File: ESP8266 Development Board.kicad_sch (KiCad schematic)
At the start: 21 parts, among them J1 Barrel_Jack, J2 Conn_01x01_Female, J3 Conn_01x01_Female, SW1 SW_SPST, SW2 SW_Push, U1 ESP8266-12E_Dev_Board

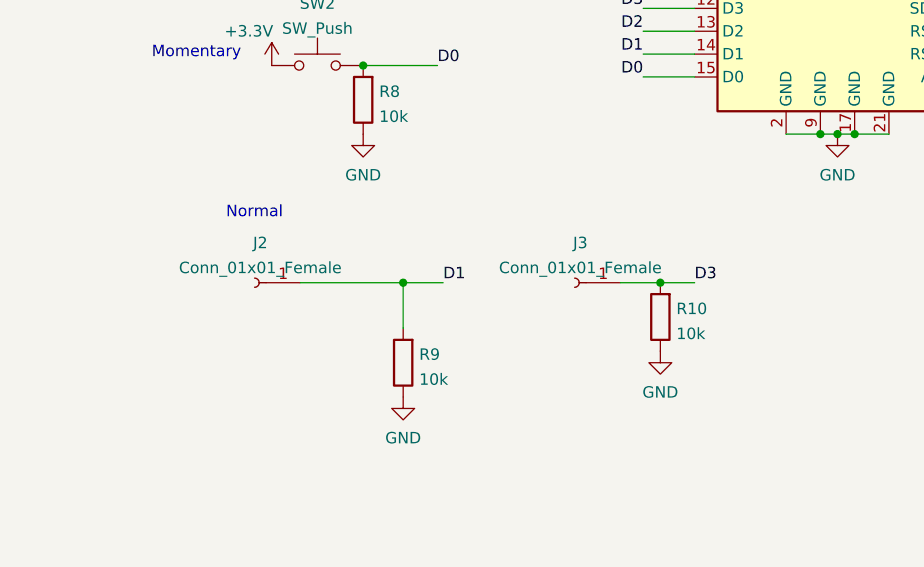
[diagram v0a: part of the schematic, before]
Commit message: Added JST headers
Added JST headers with ground points and cool 3D models
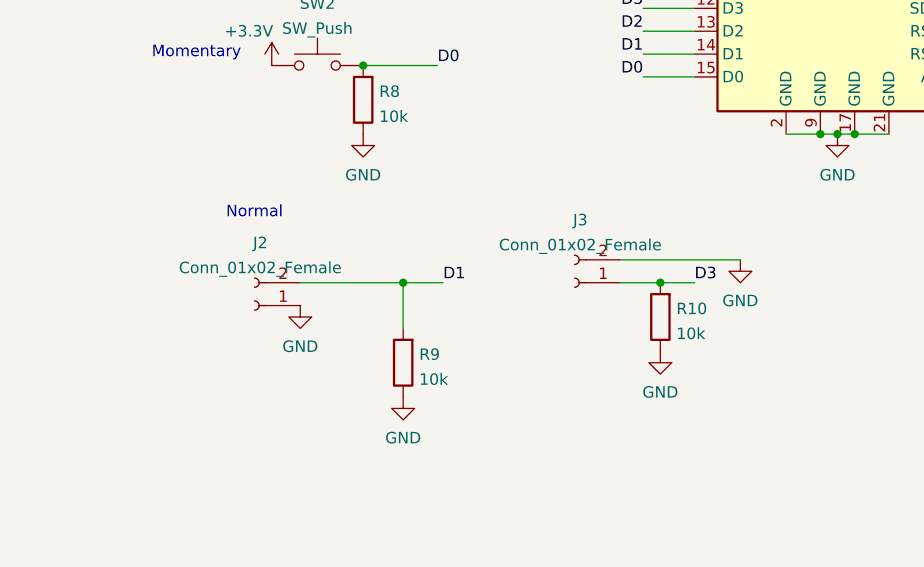
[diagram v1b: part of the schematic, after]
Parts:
- removed J2, J3: Conn_01x01_Female, Connector_PinHeader_2.54mm:PinHeader_1x01_P2.54mm_Vertical, symbol Connector:Conn_01x01_Female
- added J2, J3: Conn_01x02_Female, Connector_JST:JST_EH_B2B-EH-A_1x02_P2.50mm_Vertical, symbol Connector:Conn_01x02_Female
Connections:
- net D1: now also J2.2 (Pin_2)
- net D3: now also J3.1 (Pin_1)
- net GND: now also J2.1 (Pin_1), J3.2 (Pin_2)
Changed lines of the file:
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@@
+    (stroke (width 0) (type default) (color 0 0 0 0))
+  )
+  (wire (pts (xy 201.93 91.44) (xy 215.265 91.44))
     (stroke (width 0) (type default) (color 0 0 0 0))
   )
@@
     (pin "1")
   )
+  (symbol (lib_id "power:GND") (at 215.265 91.44 0) (unit 1)
+    (in_bom yes) (on_board yes) (fields_autoplaced)
+    (property "Reference" "#PWR0112" (id 0) (at 215.265 97.79 0)
+      (effects (font (size 1.27 1.27)) hide)
+    )
+    (property "Value" "GND" (id 1) (at 215.265 96.0025 0))
+    (property "Footprint" "" (id 2) (at 215.265 91.44 0)
+      (effects (font (size 1.27 1.27)) hide)
+    )
+    (property "Datasheet" "" (id 3) (at 215.265 91.44 0)
+      (effects (font (size 1.27 1.27)) hide)
+    )
+    (pin "1")
+  )
   (symbol (lib_id "Device:LED") (at 110.49 109.855 0) (unit 1)
     (in_bom yes) (on_board yes) (fields_autoplaced)
@@
     (pin "2")
   )
+  (symbol (lib_id "Connector:Conn_01x02_Female") (at 161.29 96.52 180) (unit 1)
+    (in_bom yes) (on_board yes)
+    (property "Reference" "J2" (id 0) (at 161.925 89.5563 0))
+    (property "Value" "Conn_01x02_Female" (id 1) (at 161.925 92.3314 0))
+    (property "Footprint" "Connector_JST:JST_EH_B2B-EH-A_1x02_P2.50mm_Vertical" (id 2) (at 161.29 96.52 0)
+      (effects (font (size 1.27 1.27)) hide)
+    )
+    (property "Datasheet" "~" (id 3) (at 161.29 96.52 0)
+      (effects (font (size 1.27 1.27)) hide)
+    )
+    (pin "1")
+    (pin "2")
+  )
   (symbol (lib_id "Device:R") (at 206.375 97.79 180) (unit 1)
     (in_bom yes) (on_board yes) (fields_autoplaced)
@@
     )
     (property "Datasheet" "~" (id 3) (at 114.935 73.025 0)
+      (effects (font (size 1.27 1.27)) hide)
+    )
+    (pin "1")
+    (pin "2")
+  )
+  (symbol (lib_id "Connector:Conn_01x02_Female") (at 196.85 93.98 180) (unit 1)
+    (in_bom yes) (on_board yes)
+    (property "Reference" "J3" (id 0) (at 197.485 87.0163 0))
+    (property "Value" "Conn_01x02_Female" (id 1) (at 197.485 89.7914 0))
+    (property "Footprint" "Connector_JST:JST_EH_B2B-EH-A_1x02_P2.50mm_Vertical" (id 2) (at 196.85 93.98 0)
+      (effects (font (size 1.27 1.27)) hide)
+    )
+    (property "Datasheet" "~" (id 3) (at 196.85 93.98 0)
       (effects (font (size 1.27 1.27)) hide)
     )
@@
     (pin "1")
   )
-  (symbol (lib_id "Connector:Conn_01x01_Female") (at 161.29 93.98 180) (unit 1)
-    (in_bom yes) (on_board yes) (fields_autoplaced)
-    (property "Reference" "J2" (id 0) (at 161.925 89.5563 0))
-    (property "Value" "Conn_01x01_Female" (id 1) (at 161.925 92.3314 0))
-    (property "Footprint" "Connector_PinHeader_2.54mm:PinHeader_1x01_P2.54mm_Vertical" (id 2) (at 161.29 93.98 0)
-      (effects (font (size 1.27 1.27)) hide)
-    )
-    (property "Datasheet" "~" (id 3) (at 161.29 93.98 0)
-      (effects (font (size 1.27 1.27)) hide)
-    )
-    (pin "1")
-  )
   (symbol (lib_id "Switch:SW_SPST") (at 66.675 61.595 0) (unit 1)
     (in_bom yes) (on_board yes) (fields_autoplaced)
@@
     (pin "1")
   )
-  (symbol (lib_id "Connector:Conn_01x01_Female") (at 196.85 93.98 180) (unit 1)
-    (in_bom yes) (on_board yes) (fields_autoplaced)
-    (property "Reference" "J3" (id 0) (at 197.485 89.5563 0))
-    (property "Value" "Conn_01x01_Female" (id 1) (at 197.485 92.3314 0))
-    (property "Footprint" "Connector_PinHeader_2.54mm:PinHeader_1x01_P2.54mm_Vertical" (id 2) (at 196.85 93.98 0)
-      (effects (font (size 1.27 1.27)) hide)
-    )
-    (property "Datasheet" "~" (id 3) (at 196.85 93.98 0)
+  (symbol (lib_id "power:GND") (at 166.37 96.52 0) (unit 1)
+    (in_bom yes) (on_board yes) (fields_autoplaced)
+    (property "Reference" "#PWR0111" (id 0) (at 166.37 102.87 0)
+      (effects (font (size 1.27 1.27)) hide)
+    )
+    (property "Value" "GND" (id 1) (at 166.37 101.0825 0))
+    (property "Footprint" "" (id 2) (at 166.37 96.52 0)
+      (effects (font (size 1.27 1.27)) hide)
+    )
+    (property "Datasheet" "" (id 3) (at 166.37 96.52 0)
       (effects (font (size 1.27 1.27)) hide)
     )
@@
       (reference "#PWR0110") (unit 1) (value "+3.3V") (footprint "")
     )
+    (path "/e0a054a6-5d83-4b6c-90f3-9d2a3890d0d3"
+      (reference "#PWR0111") (unit 1) (value "GND") (footprint "")
+    )
+    (path "/0be308a2-ed36-4877-9b9d-5acb8f594a2b"
+      (reference "#PWR0112") (unit 1) (value "GND") (footprint "")
+    )
     (path "/ea379e20-bd88-4a62-91a2-28ec4b7b876e"
       (reference "D1") (unit 1) (value "LED") (footprint "LED_THT:LED_D5.0mm")
@@
       (reference "J1") (unit 1) (value "Barrel_Jack") (footprint "Connector_BarrelJack:BarrelJack_CUI_PJ-063AH_Horizontal")
     )
-    (path "/afbd55bf-7cba-47cb-9c68-bab1b2e95ff8"
-      (reference "J2") (unit 1) (value "Conn_01x01_Female") (footprint "Connector_PinHeader_2.54mm:PinHeader_1x01_P2.54mm_Vertical")
-    )
-    (path "/e18d87ec-85b3-4253-a337-ff2935590f72"
-      (reference "J3") (unit 1) (value "Conn_01x01_Female") (footprint "Connector_PinHeader_2.54mm:PinHeader_1x01_P2.54mm_Vertical")
+    (path "/264dd9e4-b78e-4ffa-a984-843578879636"
+      (reference "J2") (unit 1) (value "Conn_01x02_Female") (footprint "Connector_JST:JST_EH_B2B-EH-A_1x02_P2.50mm_Vertical")
+    )
+    (path "/2b7b84cf-39fb-4246-99c7-76a634e84575"
+      (reference "J3") (unit 1) (value "Conn_01x02_Female") (footprint "Connector_JST:JST_EH_B2B-EH-A_1x02_P2.50mm_Vertical")
     )
     (path "/29c1e373-799b-46c4-b339-3a0a804ce479"
